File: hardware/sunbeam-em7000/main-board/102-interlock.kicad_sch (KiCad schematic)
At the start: 29 parts, among them K201 HF115F-Q/005-1H, Q201 NX3008NBK, Q202 NX3008NBK, U201 74AHCT1G17

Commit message: fix(hardware): state the catalogue number none on the hand-fitted symbols, class the 75 V resistors and enable the project's ERC and board checks [SOL-HW-MAIN-BOARD-SCHEMATIC-PROVEN.C2, .C7]
Co-Authored-By: Claude Sonnet 5.5 <noreply@anthropic.com>
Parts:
- K201, TP201, TP202, TP203, TP204, TP205, TP206: LCSC (none) -> none
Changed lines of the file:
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@@
 			)
 		)
-		(property "LCSC" ""
+		(property "LCSC" "none"
 			(at 38.1 63.5 0)
 			(hide yes)
@@
 			)
 		)
-		(property "LCSC" ""
+		(property "LCSC" "none"
 			(at 139.7 63.5 0)
 			(hide yes)
@@
 			)
 		)
-		(property "LCSC" ""
+		(property "LCSC" "none"
 			(at 228.6 101.6 0)
 			(hide yes)
@@
 			)
 		)
-		(property "LCSC" ""
+		(property "LCSC" "none"
 			(at 228.6 177.8 0)
 			(hide yes)
@@
 			)
 		)
-		(property "LCSC" ""
+		(property "LCSC" "none"
 			(at 381 101.6 0)
 			(hide yes)
@@
 			)
 		)
-		(property "LCSC" ""
+		(property "LCSC" "none"
 			(at 368.3 152.4 0)
 			(hide yes)
@@
 			)
 		)
-		(property "LCSC" ""
+		(property "LCSC" "none"
 			(at 368.3 63.5 0)
 			(hide yes)

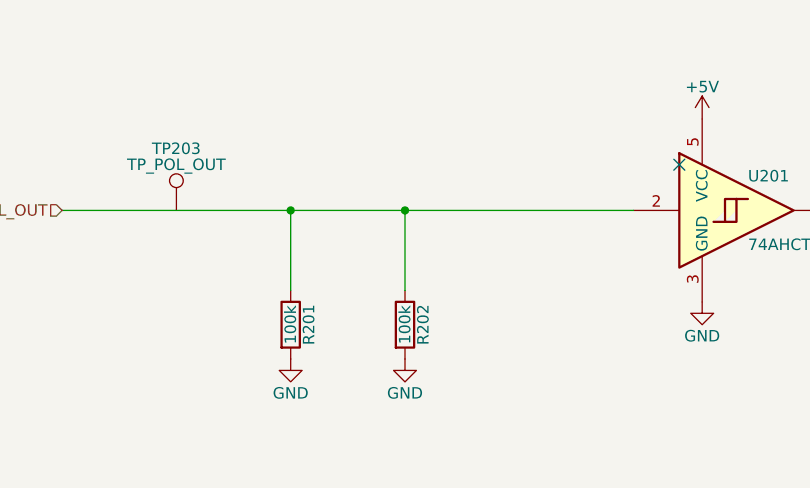
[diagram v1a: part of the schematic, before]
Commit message: feat(hardware): close the unpowered-buffer finding with a series resistor in the polarity line [SOL-HW-MAIN-BOARD-SCHEMATIC-PROVEN.C1, .C2, .C5]
Co-Authored-By: Claude Sonnet 5.5 <noreply@anthropic.com>
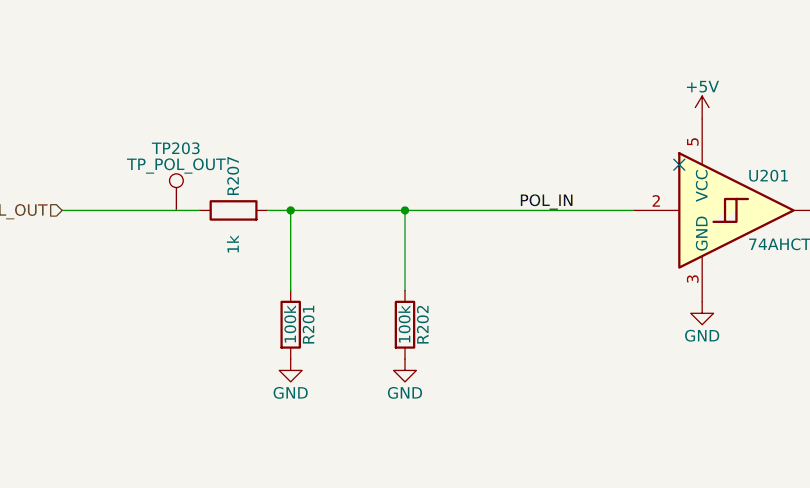
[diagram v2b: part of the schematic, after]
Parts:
- added R207: 1k, Resistor_SMD:R_0603_1608Metric, symbol Device:R
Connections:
- net POL_OUT: now also R207.1; no longer R201.1, R202.1, U201.2
- new net POL_IN: R201.1, R202.1, R207.2, U201.2

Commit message: fix(hardware): move the symbols with mismatched footprint filters into the board's own library [SOL-HW-MAIN-BOARD-SCHEMATIC-PROVEN.C2, .C7]
Co-Authored-By: Claude Sonnet 5.5 <noreply@anthropic.com>
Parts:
- D202, D204, D205, D206: symbol Diode:BAS16W -> main-board:BAS16W
- K201: symbol Relay:Relay_SPST-NO -> main-board:Relay_SPST-NO
- U201: symbol 74xGxx:74LVC1G17 -> main-board:74LVC1G17
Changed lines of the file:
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@@
 	)
 	(symbol
-		(lib_id "74xGxx:74LVC1G17")
+		(lib_id "main-board:74LVC1G17")
 		(at 101.6 63.5 0)
 		(unit 1)
@@
 	)
 	(symbol
-		(lib_id "Diode:BAS16W")
+		(lib_id "main-board:BAS16W")
 		(at 203.2 114.3 0)
 		(unit 1)
@@
 	)
 	(symbol
-		(lib_id "Diode:BAS16W")
+		(lib_id "main-board:BAS16W")
 		(at 203.2 190.5 0)
 		(unit 1)
@@
 	)
 	(symbol
-		(lib_id "Diode:BAS16W")
+		(lib_id "main-board:BAS16W")
 		(at 342.9 127 0)
 		(unit 1)
@@
 	)
 	(symbol
-		(lib_id "Diode:BAS16W")
+		(lib_id "main-board:BAS16W")
 		(at 342.9 165.1 0)
 		(unit 1)
@@
 	)
 	(symbol
-		(lib_id "Relay:Relay_SPST-NO")
+		(lib_id "main-board:Relay_SPST-NO")
 		(at 381 101.6 0)
 		(unit 1)

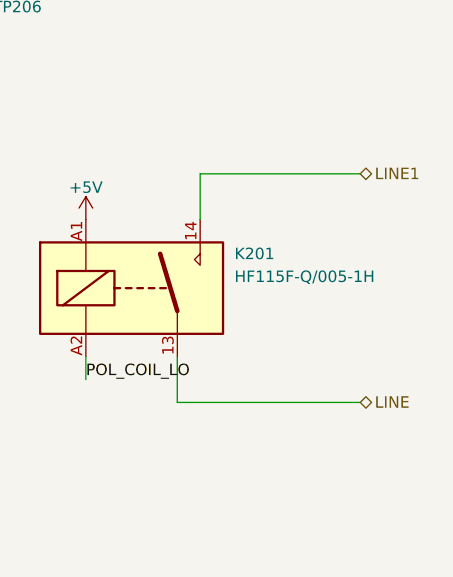
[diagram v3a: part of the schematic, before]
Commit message: feat(hardware): swap the relay's two contact nets to match the tab order and rebalance the floorplan to the real part sizes [SOL-HW-MAIN-BOARD-PROVEN-AND-LAID-OUT.C7, .C14]
Co-Authored-By: Claude Sonnet 5.5 <noreply@anthropic.com>
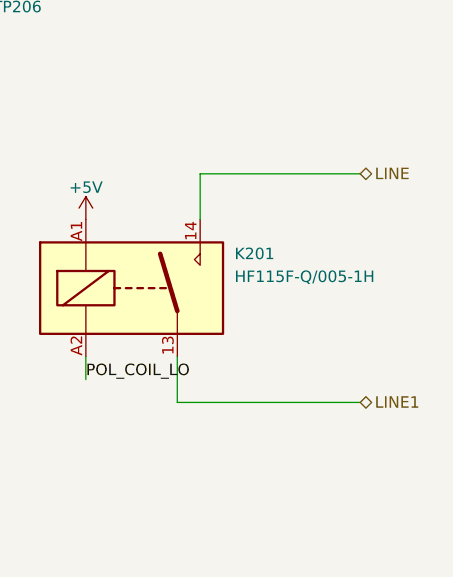
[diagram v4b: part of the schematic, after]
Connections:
- net LINE: now also K201.14; no longer K201.13
- net LINE1: now also K201.13; no longer K201.14
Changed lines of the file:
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@@
 		)
 	)
-	(hierarchical_label "LINE"
+	(hierarchical_label "LINE1"
 		(shape bidirectional)
 		(at 406.4 114.3 0)
@@
 		)
 	)
-	(hierarchical_label "LINE1"
+	(hierarchical_label "LINE"
 		(shape bidirectional)
 		(at 406.4 88.9 0)

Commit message: main-board: point the 96 test-point symbols and Y601 at the small test-point and marked oscillator footprints [SOL-HW-MAIN-BOARD-PROVEN-AND-LAID-OUT.C8]
Co-Authored-By: Claude Sonnet 5.5 <noreply@anthropic.com>
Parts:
- TP201, TP202, TP203, TP204, TP205, TP206: footprint TestPoint:TestPoint_Pad_D1.5mm -> main-board:TestPoint_Pad_D1.0mm_Tight
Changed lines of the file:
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@@
 			)
 		)
-		(property "Footprint" "TestPoint:TestPoint_Pad_D1.5mm"
+		(property "Footprint" "main-board:TestPoint_Pad_D1.0mm_Tight"
 			(at 38.1 63.5 0)
 			(hide yes)
@@
 			)
 		)
-		(property "Footprint" "TestPoint:TestPoint_Pad_D1.5mm"
+		(property "Footprint" "main-board:TestPoint_Pad_D1.0mm_Tight"
 			(at 139.7 63.5 0)
 			(hide yes)
@@
 			)
 		)
-		(property "Footprint" "TestPoint:TestPoint_Pad_D1.5mm"
+		(property "Footprint" "main-board:TestPoint_Pad_D1.0mm_Tight"
 			(at 228.6 101.6 0)
 			(hide yes)
@@
 			)
 		)
-		(property "Footprint" "TestPoint:TestPoint_Pad_D1.5mm"
+		(property "Footprint" "main-board:TestPoint_Pad_D1.0mm_Tight"
 			(at 228.6 177.8 0)
 			(hide yes)
@@
 			)
 		)
-		(property "Footprint" "TestPoint:TestPoint_Pad_D1.5mm"
+		(property "Footprint" "main-board:TestPoint_Pad_D1.0mm_Tight"
 			(at 368.3 152.4 0)
 			(hide yes)
@@
 			)
 		)
-		(property "Footprint" "TestPoint:TestPoint_Pad_D1.5mm"
+		(property "Footprint" "main-board:TestPoint_Pad_D1.0mm_Tight"
 			(at 368.3 63.5 0)
 			(hide yes)
